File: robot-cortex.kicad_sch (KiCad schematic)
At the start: 43 parts, among them IC1 THVD2410VDRCR, J1 USB4110GFA, M1 THRU_HOLE_PAD, M2 THRU_HOLE_PAD, U1 C2901617, U2 STM32G431CBT6, U3 TLE9250XSJXUMA1, U4 DF52-3S-0.8H(21), U5 DF52-4S-0.8H(21), U6 SPX3819M5-L-5-0

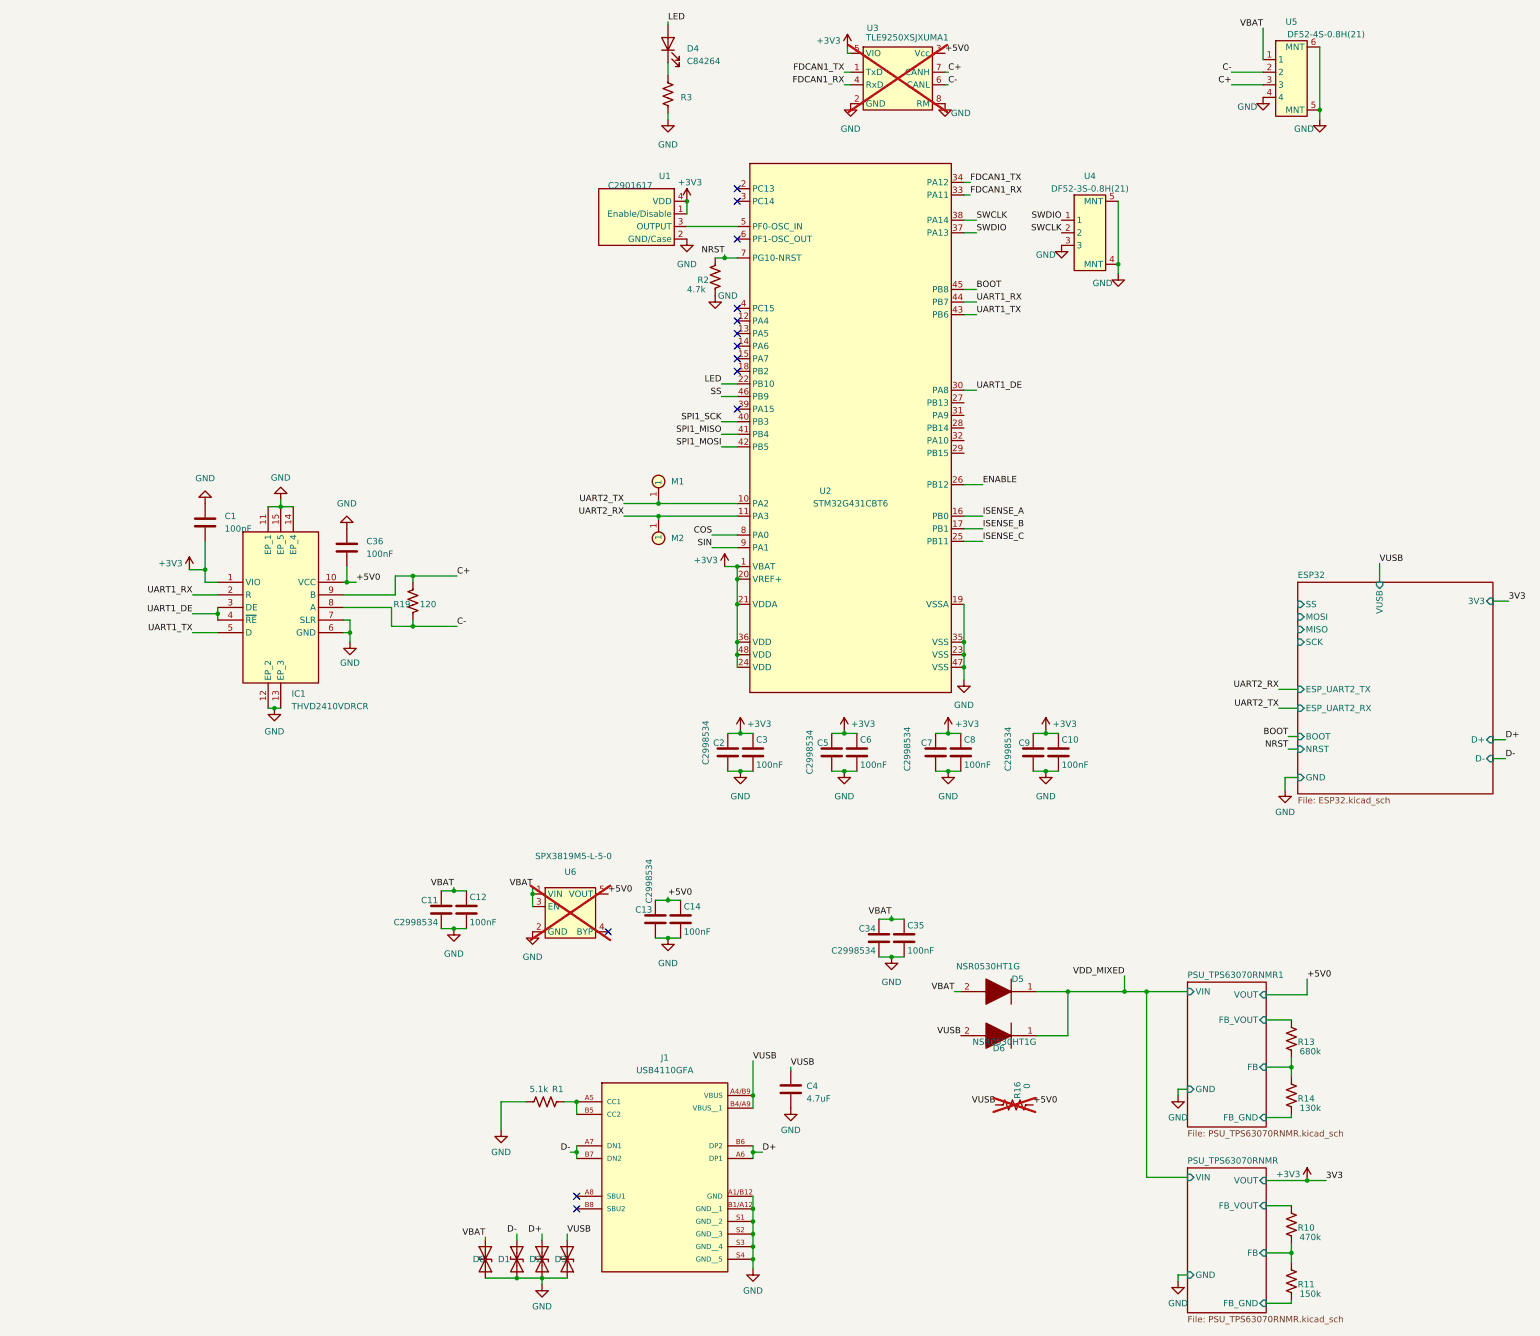
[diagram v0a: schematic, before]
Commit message: updates to design - including new uart channels and rs485 channels
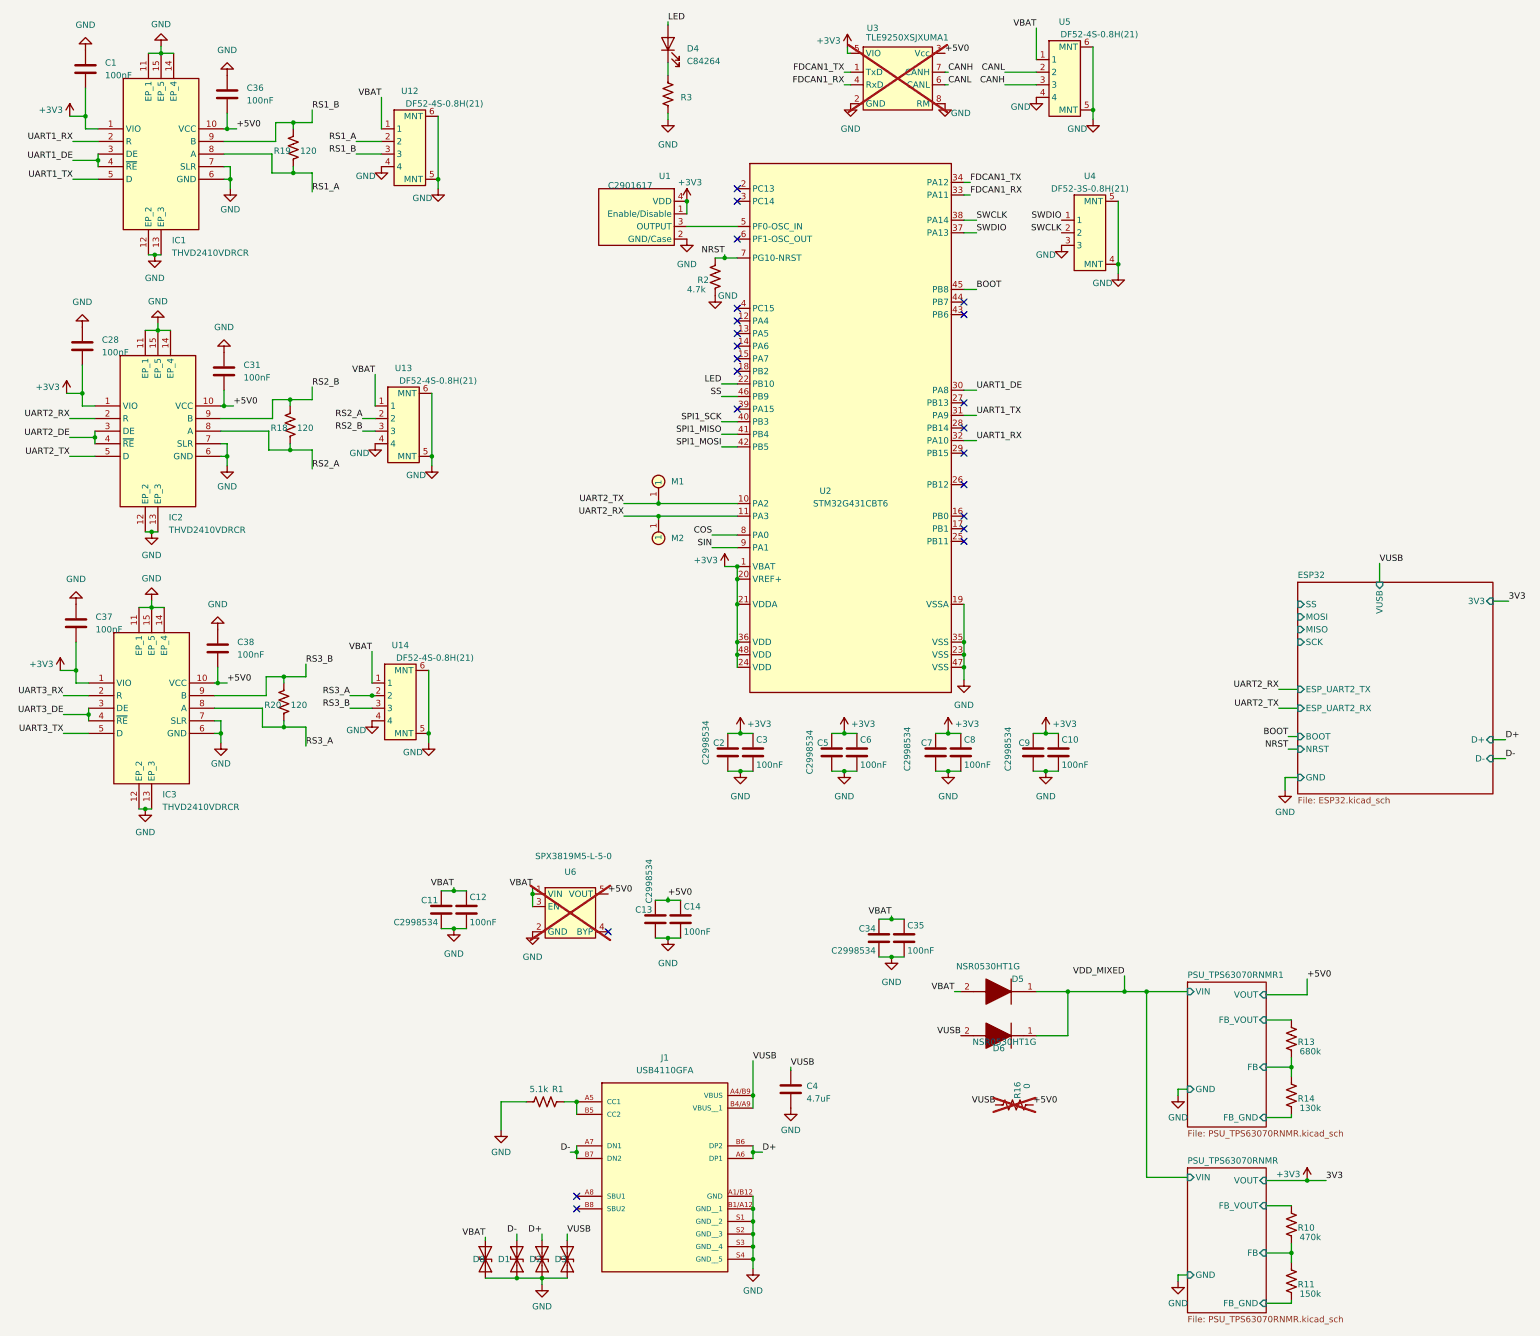
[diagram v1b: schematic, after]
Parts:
- added C28, C31, C37, C38: 100nF, Capacitor_SMD:C_0402_1005Metric, symbol Device:C
- added IC2, IC3: THVD2410VDRCR, robot-cortex:THVD2410VDRCR, symbol SamacSys_Parts:THVD2410VDRCR
- added R18, R20: 120, robot-cortex:R_0402_1005Metric, symbol robot-cortex:R
- added U12, U13, U14: DF52-4S-0.8H(21), robot-cortex:DF52-4S-0.8H(21), symbol foc-pcb:DF52-4S-0.8H(21)
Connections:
- net +3V3: now also C28.2, C37.2, IC2.1 (VIO), IC3.1 (VIO)
- net +5V0: now also C31.2, C38.2, IC2.10 (VCC), IC3.10 (VCC)
- net GND: now also C28.1, C31.1, C37.1, C38.1, IC2.11 (EP_1), IC2.12 (EP_2), IC2.13 (EP_3), IC2.14 (EP_4), IC2.15 (EP_5), IC2.6 (GND), IC2.7 (SLR), IC3.11 (EP_1), IC3.12 (EP_2), IC3.13 (EP_3), IC3.14 (EP_4), IC3.15 (EP_5), IC3.6 (GND), IC3.7 (SLR), U12.4, U12.5 (MNT), U12.6 (MNT), U13.4, U13.5 (MNT), U13.6 (MNT), U14.4, U14.5 (MNT), U14.6 (MNT)
- net UART1_RX: now also U2.32 (PA10); no longer U2.44 (PB7)
- net UART1_TX: now also U2.31 (PA9); no longer U2.43 (PB6)
- net UART2_RX: now also IC2.2 (R)
- net UART2_TX: now also IC2.5 (D)
- net VBAT: now also U12.1, U13.1, U14.1
- net C+ renamed CANH
- net CANH: no longer IC1.9 (B), R19.2
- net C- renamed CANL
- net CANL: no longer IC1.8 (A), R19.1
- net ENABLE: no longer names the net of U2.26 (PB12)
- net ISENSE_A: no longer names the net of U2.16 (PB0)
- net ISENSE_B: no longer names the net of U2.17 (PB1)
- net ISENSE_C: no longer names the net of U2.25 (PB11)
- new net RS1_A: IC1.8 (A), R19.1, U12.2
- new net RS1_B: IC1.9 (B), R19.2, U12.3
- new net RS2_A: IC2.8 (A), R18.1, U13.2
- new net RS2_B: IC2.9 (B), R18.2, U13.3
- new net RS3_A: IC3.8 (A), R20.1, U14.2
- new net RS3_B: IC3.9 (B), R20.2, U14.3
- new net UART2_DE: IC2.3 (DE), IC2.4 (~{RE})
- new net UART3_DE: IC3.3 (DE), IC3.4 (~{RE})
- new net UART3_RX: IC3.2 (R)
- new net UART3_TX: IC3.5 (D)
- no-connect marks 13 -> 22
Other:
- moved on the sheet: C1, C36, IC1, R19, U5

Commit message: updates to pins, layout
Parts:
- removed C1, C28, C31, C36, C37, C38: 100nF, Capacitor_SMD:C_0402_1005Metric, symbol Device:C
- removed IC1, IC2, IC3: THVD2410VDRCR, robot-cortex:THVD2410VDRCR, symbol SamacSys_Parts:THVD2410VDRCR
- removed R18, R19, R20: 120, robot-cortex:R_0402_1005Metric, symbol robot-cortex:R
- removed U12, U13, U14: DF52-4S-0.8H(21), robot-cortex:DF52-4S-0.8H(21), symbol foc-pcb:DF52-4S-0.8H(21)
- added R18: 4.7k, robot-cortex:R_0402_1005Metric, symbol foc-pcb:Resistor
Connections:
- net BOOT: now also R18.1
- net GND: now also R18.2
- net LED: now also U2.17 (PB1); no longer U2.22 (PB10)
- net SS: now also U2.39 (PA15); no longer U2.46 (PB9)
- net UART3_RX: now also U2.25 (PB11)
- net UART3_TX: now also U2.22 (PB10)
- net I2S2_WS: now reaches U2.26 (PB12)
- net I2S2_CK: now reaches U2.27 (PB13)
- net USART3_DE: now reaches U2.28 (PB14)
- net I2S2_SD: now reaches U2.29 (PB15)
- net COS: no longer names the net of U2.8 (PA0)
- net SIN renamed USART2_DE
- no-connect marks 22 -> 17
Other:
- added sheet RS485 Transceiver (RS485-Transceiver.kicad_sch)
- added sheet RS485 Transceiver1 (RS485-Transceiver.kicad_sch)
- added sheet RS485 Transceiver2 (RS485-Transceiver.kicad_sch)
- moved on the sheet: U1

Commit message: fix vbat
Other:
- sheet RS485 Transceiver ports: added VBAT; removed none
- sheet RS485 Transceiver1 ports: added VBAT; removed none
- sheet RS485 Transceiver2 ports: added VBAT; removed none

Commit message: routed, gotta check da pinz
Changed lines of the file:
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@@
-    (effects (font (size 1.27 1.27)) (justify right bottom))
-  )
-  (label "SPI1_MOSI" (at 272.415 145.415 180) (fields_autoplaced)
     (effects (font (size 1.27 1.27)) (justify right bottom))
   )
@@
     (effects (font (size 1.27 1.27)) (justify left bottom))
   )
+  (label "SPI1_SCK" (at 272.415 145.415 180) (fields_autoplaced)
+    (effects (font (size 1.27 1.27)) (justify right bottom))
+  )
   (label "USART3_DE" (at 208.915 102.235 0) (fields_autoplaced)
     (effects (font (size 1.27 1.27)) (justify left bottom))
+  )
+  (label "SPI1_MOSI" (at 272.415 140.335 180) (fields_autoplaced)
+    (effects (font (size 1.27 1.27)) (justify right bottom))
   )
   (label "SPI1_MOSI" (at 157.48 106.045 180) (fields_autoplaced)
@@
     (effects (font (size 1.27 1.27)) (justify left bottom))
   )
-  (label "SPI1_SCK" (at 272.415 140.335 180) (fields_autoplaced)
-    (effects (font (size 1.27 1.27)) (justify right bottom))
-  )
   (label "FDCAN1_RX" (at 182.245 33.02 180) (fields_autoplaced)

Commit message: bom cleanup - caps not hardcoded lcsc part, led replaced
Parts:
- C11, C13, C2, C34, C5, C7, C9: value C2998534 -> 10uF 0603; Voltage (none) -> 10V
- D4: value C84264 -> 150060GS84000
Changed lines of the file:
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@@
       (effects (font (size 1.27 1.27)) (justify left))
     )
-    (property "Value" "C2998534" (at 154.305 170.18 90)
+    (property "Value" "10uF 0603" (at 153.67 172.72 90)
       (effects (font (size 1.27 1.27)) (justify left))
     )
@@
       (effects (font (size 1.27 1.27)) hide)
     )
+    (property "Voltage" "10V" (at 171.45 186.69 90)
+      (effects (font (size 1.27 1.27)) (justify left) hide)
+    )
     (pin "1")
     (pin "2")
@@
       (effects (font (size 1.27 1.27)) (justify left))
     )
-    (property "Value" "C2998534" (at 175.26 172.085 90)
+    (property "Value" "10uF 0603" (at 175.26 172.72 90)
       (effects (font (size 1.27 1.27)) (justify left))
     )
@@
     (property "Datasheet" "~" (at 179.705 167.64 0)
       (effects (font (size 1.27 1.27)) hide)
+    )
+    (property "Voltage" "10V" (at 177.8 172.72 90)
+      (effects (font (size 1.27 1.27)) (justify left) hide)
     )
     (pin "1")
@@
       (effects (font (size 1.27 1.27)) (justify left))
     )
-    (property "Value" "C2998534" (at 215.265 171.45 90)
+    (property "Value" "10uF 0603" (at 215.9 172.72 90)
       (effects (font (size 1.27 1.27)) (justify left))
     )
@@
     (property "Datasheet" "~" (at 220.345 167.64 0)
       (effects (font (size 1.27 1.27)) hide)
+    )
+    (property "Voltage" "10V" (at 194.945 171.45 90)
+      (effects (font (size 1.27 1.27)) (justify left) hide)
     )
     (pin "1")
@@
       (effects (font (size 1.27 1.27)) (justify left))
     )
-    (property "Value" "C2998534" (at 142.875 198.12 90)
+    (property "Value" "10uF 0603" (at 140.97 208.28 90)
       (effects (font (size 1.27 1.27)) (justify left))
     )
@@
     (property "Datasheet" "~" (at 144.145 201.295 0)
       (effects (font (size 1.27 1.27)) hide)
+    )
+    (property "Voltage" "10V" (at 191.77 181.61 90)
+      (effects (font (size 1.27 1.27)) (justify left) hide)
     )
     (pin "1")
@@
       (effects (font (size 1.27 1.27)) (justify left))
     )
-    (property "Value" "C2998534" (at 188.595 207.645 0)
+    (property "Value" "10uF 0603" (at 184.15 212.09 90)
       (effects (font (size 1.27 1.27)) (justify left))
     )
@@
     (property "Datasheet" "~" (at 189.23 205.105 0)
       (effects (font (size 1.27 1.27)) hide)
+    )
+    (property "Voltage" "10V" (at 184.15 191.77 90)
+      (effects (font (size 1.27 1.27)) (justify left) hide)
     )
     (pin "1")
@@
       (effects (font (size 1.27 1.27)) (justify right))
     )
-    (property "Value" "C84264" (at 150.495 28.2575 90)
+    (property "Value" "150060GS84000" (at 150.495 28.2575 90)
       (effects (font (size 1.27 1.27)) (justify right))
     )
@@
       (effects (font (size 1.27 1.27)) hide)
     )
-    (property "Datasheet" "~" (at 146.685 24.765 0)
+    (property "Datasheet" "https://www.we-online.com/components/products/datasheet/150060GS84000.pdf" (at 146.685 24.765 0)
       (effects (font (size 1.27 1.27)) hide)
     )
@@
       (effects (font (size 1.27 1.27)) (justify left))
     )
-    (property "Value" "C2998534" (at 100.33 201.93 0)
+    (property "Value" "10uF 0603" (at 97.79 210.82 90)
       (effects (font (size 1.27 1.27)) (justify left))
     )
@@
     (property "Datasheet" "~" (at 100.965 199.39 0)
       (effects (font (size 1.27 1.27)) hide)
+    )
+    (property "Voltage" "10V" (at 186.69 184.15 90)
+      (effects (font (size 1.27 1.27)) (justify left) hide)
     )
     (pin "1")
@@
       (effects (font (size 1.27 1.27)) (justify left))
     )
-    (property "Value" "C2998534" (at 194.945 171.45 90)
+    (property "Value" "10uF 0603" (at 199.39 184.15 90)
       (effects (font (size 1.27 1.27)) (justify left))
     )
@@
       (effects (font (size 1.27 1.27)) hide)
     )
-    (pin "1")
+    (property "Voltage" "10V" (at 190.5 184.15 90)
+      (effects (font (size 1.27 1.27)) (justify left) hide)
+    )
+    (pin "1")
